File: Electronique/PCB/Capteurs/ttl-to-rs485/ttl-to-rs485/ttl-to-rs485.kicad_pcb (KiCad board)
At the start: 2 copper layers, 62.2 x 44.5 mm, 4 parts, among them U1 HW-221, U2 JST-SH 4, U3 JST-SH4 motor, U4 TTL-RS485

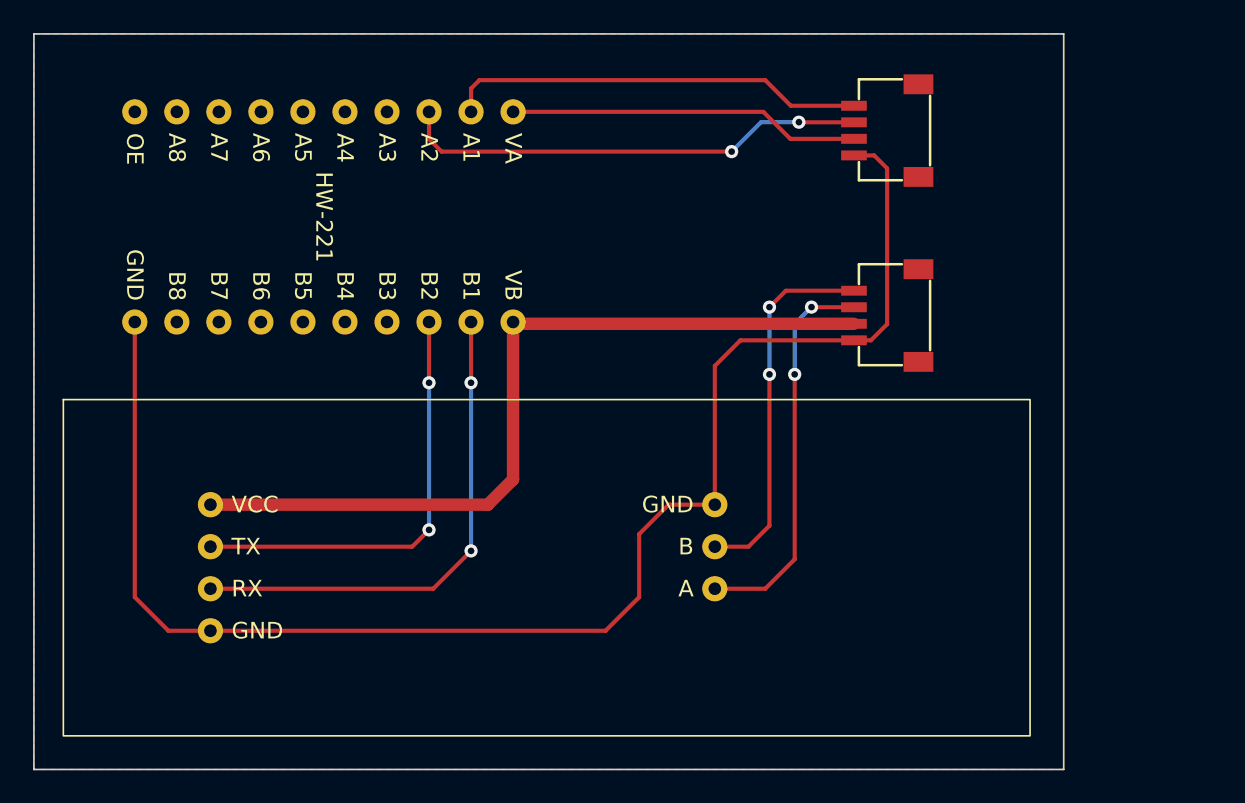
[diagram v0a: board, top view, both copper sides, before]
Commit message: update to ttl to rs485 pcb
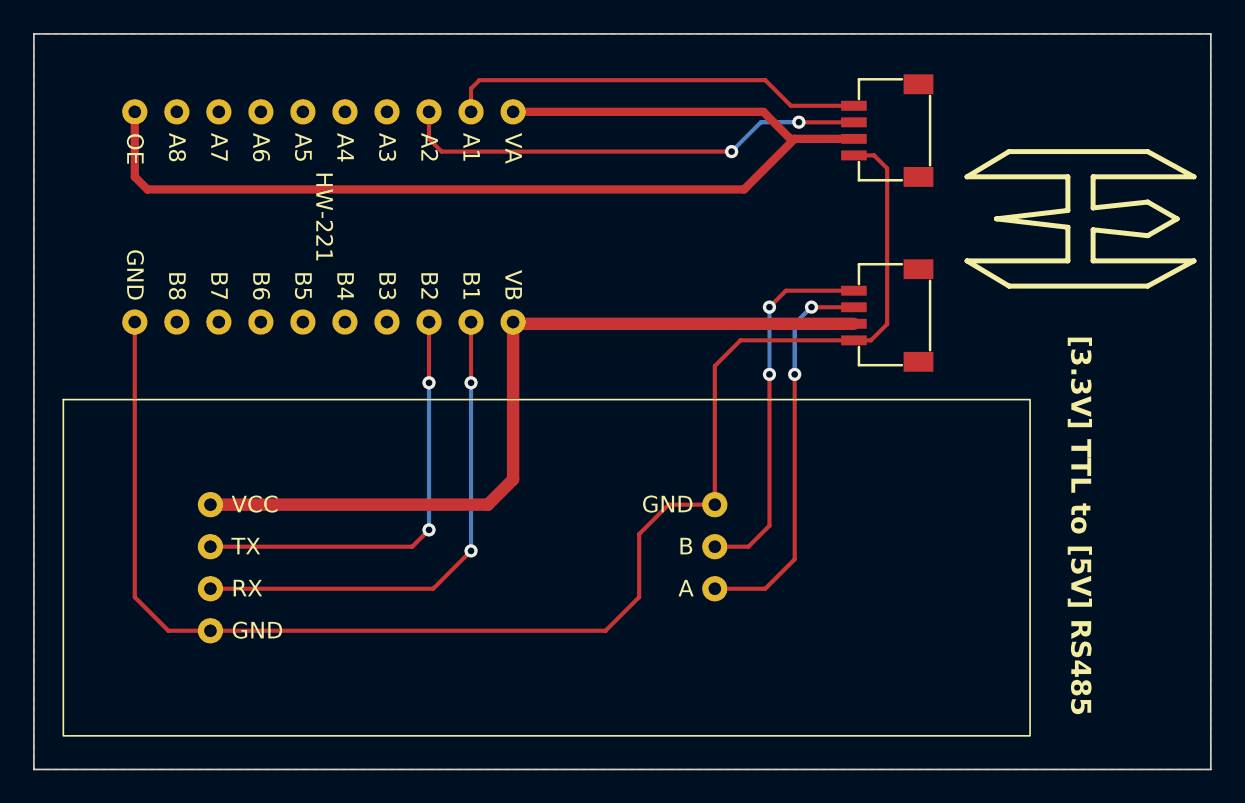
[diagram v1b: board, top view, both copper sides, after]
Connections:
- U1 pad 10: /OUT_ENABLE -> /3.3V
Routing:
- net /3.3V: track 21.3 -> 66.7 mm
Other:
- board size 62.2 x 44.5 mm -> 71.1 x 44.5 mm
- board text added: "[3.3V] TTL to [5V] RS485"
